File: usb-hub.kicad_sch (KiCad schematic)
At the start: 0 parts

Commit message: [#99658] Implement USB2.0 HUB
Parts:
- added C702, C704, C705, C706, C707, C709: C_1u_0402, antmicro-footprints:C_0402_1005Metric, symbol antmicroCapacitors0402:C_1u_0402
- added C708: C_100n_0402, antmicro-footprints:C_0402_1005Metric, symbol antmicroCapacitors0402:C_100n_0402
- added C710, C711: C_18p_0402, antmicro-footprints:C_0402_1005Metric, symbol antmicroCapacitors0402:C_18p_0402
- added R701, R704: R_10k_0402, antmicro-footprints:R_0402_1005Metric, symbol antmicroResistors0402:R_10k_0402
- added R705, R706, R708, R716, R717: R_0R_0402, antmicro-footprints:R_0402_1005Metric, symbol antmicroResistors0402:R_0R_0402
- added R707: R_1M_0402, antmicro-footprints:R_0402_1005Metric, symbol antmicroResistors0402:R_1M_0402
- added R709, R713, R714: R_100k_0402, antmicro-footprints:R_0402_1005Metric, symbol antmicroResistors0402:R_100k_0402
- added R715: R_12k_0402, antmicro-footprints:R_0402_1005Metric, symbol antmicroResistors0402:R_12k_0402
- added U701: USB2422-I_MJ, antmicro-footprints:QFN-24-1EP_4x4mm_P0.5mm_EP2.6x2.6mm, symbol antmicroInterfaceControllers:USB2422-I_MJ
- added Y702: Resonator_27.12MHz_XRCGB, antmicro-footprints:Resonator_SMD_Murata_XRCGB_2x1.6x0.65mm, symbol antmicroResonators:Resonator_24MHz_XRCGB
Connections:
- new net: C710.2, R707.2, R708.1, Y702.1
- new net: C708.2, U701.23 (PLLFILT)
- new net: R715.2, U701.24 (R_{BIAS})
- new net: C709.2, U701.10 (CRFILT)
- new net +3V3: C705.2, C706.2, C707.2, R701.1, R704.1, R713.2, U701.1 (3V3), U701.18 (3V3), U701.9 (3V3)
- new net CFG_SEL: R709.2, U701.14 (SMBCLK)
- new net DN2_D+: R716.1, U701.5 (DN2_D+)
- new net DN2_D-: R717.1, U701.4 (DN2_D-)
- new net GND: C702.1, C704.1, C705.1, C706.1, C707.1, C708.1, C709.1, C710.1, C711.1, R709.1, R714.1, R715.1, U701.25 (GND), Y702.2 (SH), Y702.4 (SH)
- new net NON_REM0: R714.2, U701.17 (SUSP_IND)
- new net NON_REM1: R713.1, U701.13 (SMBDATA)
- new net UP_D+: R705.2, U701.20 (UP_D+)
- new net UP_D-: R706.2, U701.19 (UP_D-)
- new net USB1.D+: U701.3 (DN1_D+)
- new net USB1.D-: U701.2 (DN1_D-)
- new net USB2.D+: R716.2
- new net USB2.D-: R717.2
- new net USB_HOST.D+: R705.1
- new net USB_HOST.D-: R706.1
- new net USB_HUB_2_FLG: U701.12 (OSC_{N2})
- new net USB_HUB_2_PEN: U701.11 (PWR_{PRT2})
- new net VBUS_DET: C704.2, R704.2, U701.16 (VBUS_{DET})
- new net XTAL_IN: R708.2, U701.22 (XTAL_{IN})
- new net XTAL_OUT: C711.2, R707.1, U701.21 (XTAL_{OUT}), Y702.3
- new net ~{HUB_RST}: C702.2, R701.2, U701.15 (~{RESET})
- no-connect marks 0 -> 2
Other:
- note added: "CFG_SEL = 0 Strap options enabled"
- note added: "NON_REM1 = 0, NON_REM0 = 1 Port 1 is non-removable Port 2 is removable"
- note added: "To DC-SCM connector (non-removable)"
- note added: "To USB-C connector (removable)"
- note added: "USB Hub"

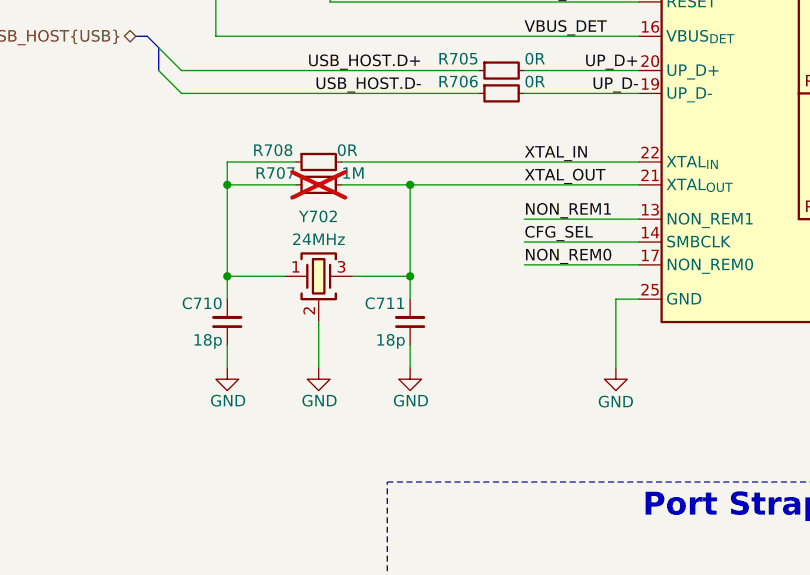
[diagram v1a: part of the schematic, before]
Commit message: [#99727] Unify 24MHz resonators
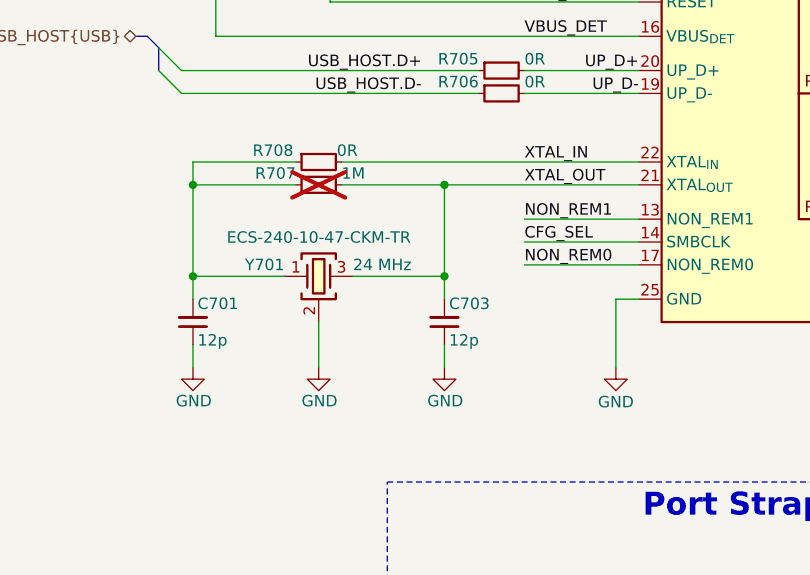
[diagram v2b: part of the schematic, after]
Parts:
- removed C710, C711: C_18p_0402, antmicro-footprints:C_0402_1005Metric, symbol antmicroCapacitors0402:C_18p_0402
- removed Y702: Resonator_27.12MHz_XRCGB, antmicro-footprints:Resonator_SMD_Murata_XRCGB_2x1.6x0.65mm, symbol antmicroResonators:Resonator_24MHz_XRCGB
- added C701, C703: C_12p_0402, antmicro-footprints:C_0402_1005Metric, symbol antmicroCapacitors0402:C_12p_0402
- added Y701: Resonator_24MHz_ECX-1247, antmicro-footprints:Resonator_SMD_ECS_ECX-1247_1.6x1.2x0.3mm, symbol antmicroResonators:Resonator_24MHz_ECX-1247
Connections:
- net GND: now also C701.1, C703.1, Y701.2 (SH), Y701.4 (SH)
- net XTAL_OUT: now also C703.2, Y701.3
- net at R707.2, R708.1: now also C701.2, Y701.1
